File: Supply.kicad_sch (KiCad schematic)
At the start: 14 parts, among them IC1 B1212S-2W, IC3 JW5052C

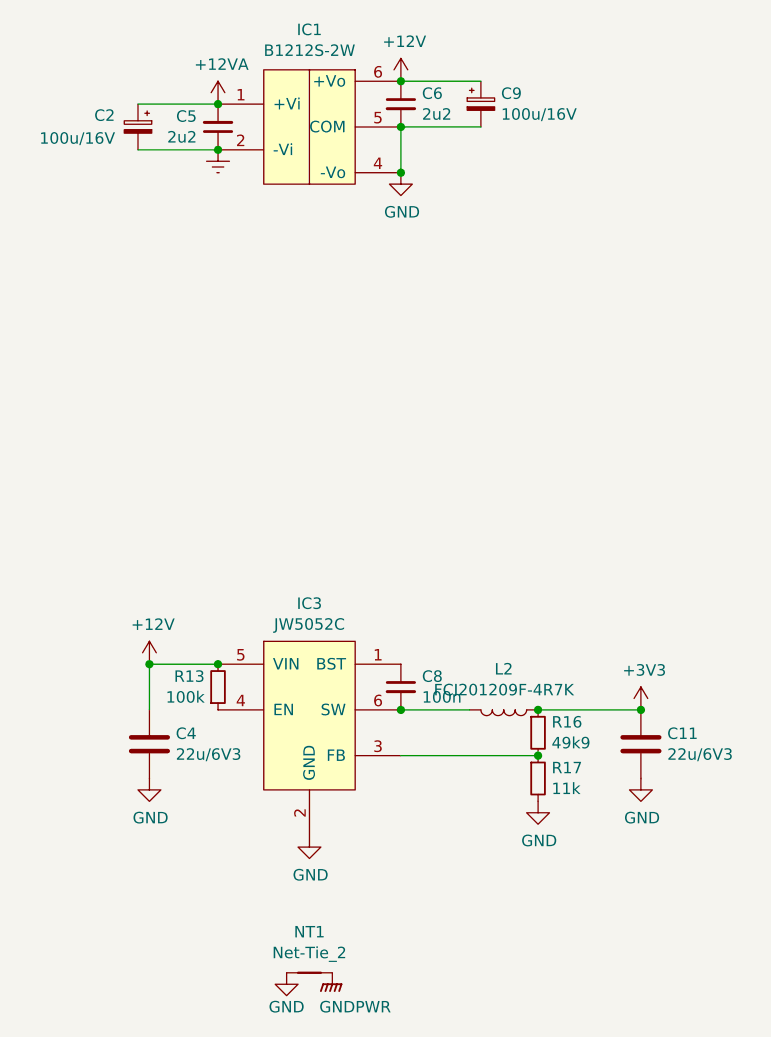
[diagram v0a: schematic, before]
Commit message: - peeled back the filler planes around HV logic - improved insulation on HV logic
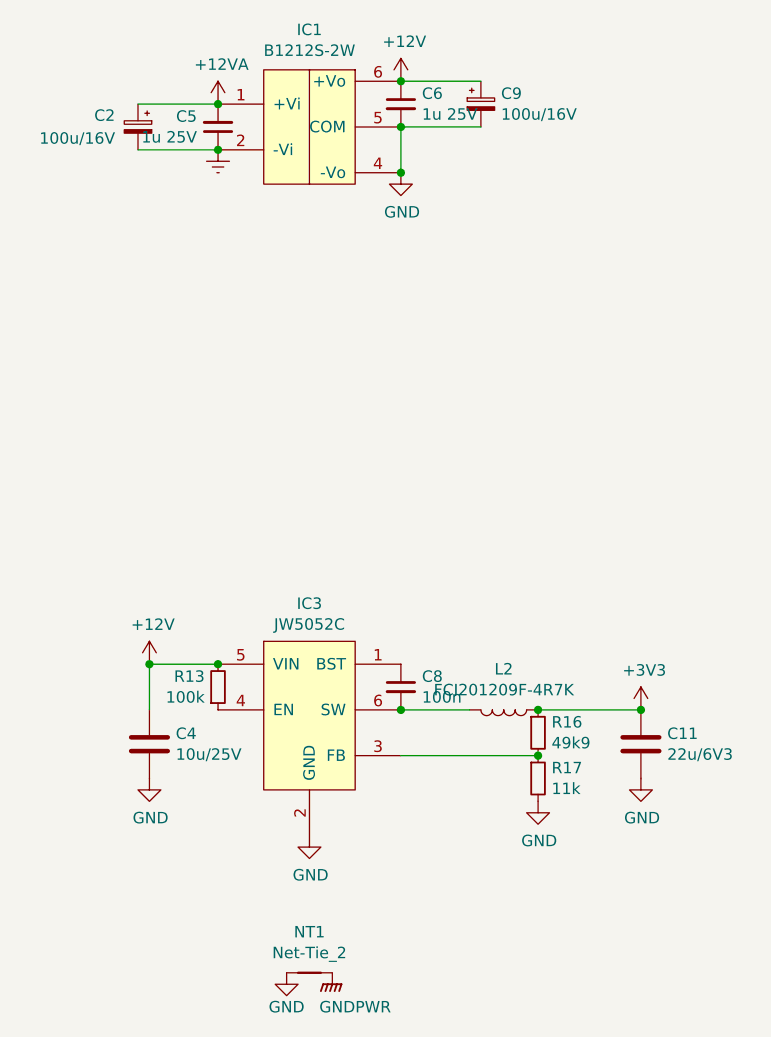
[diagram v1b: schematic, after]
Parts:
- C4: value 22u/6V3 -> 10u/25V
- C5, C6: value 2u2 -> 1u 25V
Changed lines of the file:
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@@
       (effects (font (size 1.27 1.27)) (justify left))
     )
-    (property "Value" "22u/6V3" (at 82.931 143.383 0)
+    (property "Value" "10u/25V" (at 82.931 143.383 0)
       (effects (font (size 1.27 1.27)) (justify left))
     )
@@
       (effects (font (size 1.27 1.27)) (justify right))
     )
-    (property "Value" "2u2" (at 85.2932 74.803 0)
+    (property "Value" "1u 25V" (at 85.2932 74.803 0)
       (effects (font (size 1.27 1.27)) (justify right))
     )
@@
       (effects (font (size 1.27 1.27)) (justify left))
     )
-    (property "Value" "2u2" (at 110.2868 72.263 0)
+    (property "Value" "1u 25V" (at 110.2868 72.263 0)
       (effects (font (size 1.27 1.27)) (justify left))
     )
